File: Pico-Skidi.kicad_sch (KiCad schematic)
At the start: 10 parts, among them M1 Motor_DC, M2 Motor_DC, M3 Motor_DC, M4 Motor_Servo, M5 Motor_Servo, U1 Pico, U2 PDRV8411PWPR, U3 PDRV8411PWPR, U4 LM5156HPWPR

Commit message: Starting on Power
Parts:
- added C1: 10uf, symbol Device:C
- added D1: LED, symbol Device:LED
- added J1: BAT, symbol Connector_Generic:Conn_01x02
- added J2: RGBLED, symbol Connector_Generic:Conn_01x03
- added J3: USB_C_Receptacle, symbol Connector:USB_C_Receptacle
- added R1, R2: 5k1, symbol Device:R
- added R3: 2k, symbol Device:R
- added U5: MCP73831T-2ACI/OT, SOT-23-5_MC_MCH, symbol MCP73831:MCP73831T-2ACI_OT
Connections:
- net GND: now reaches U2.11 (GND)
- net GND: now also M4.3 (-), M5.3 (-), U1.13 (GND), U1.18 (GND), U1.23 (GND), U1.28 (GND), U1.3 (GND), U1.33 (AGND), U1.38 (GND), U1.42 (GND), U1.8 (GND), U3.11 (GND), C1.2, J2.3 (Pin_3), J3.A1 (GND), J3.A12 (GND), J3.B1 (GND), J3.B12 (GND), J3.S1 (SHIELD), R1.2, R2.2, U5.2 (VSS)
- new net: D1.1 (K), R3.1
- new net: J3.A5 (CC1), R2.1
- new net: J3.B5 (CC2), R1.1
- new net: R3.2, U5.1 (STAT)
- new net: J1.1 (Pin_1), U5.3 (VBAT)
- new net D+: J3.A6 (D+), J3.B6 (D+)
- new net D-: J3.A7 (D-), J3.B7 (D-)
- new net VBUS: C1.1, D1.2 (A), J3.A4 (VBUS), J3.A9 (VBUS), J3.B4 (VBUS), J3.B9 (VBUS), U5.4 (VDD)
- no-connect marks 0 -> 10
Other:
- moved on the sheet: M1, M2, M3, M4, M5, U1, U2, U3, U4

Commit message: Sync
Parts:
- added R4, R5: R, symbol Device:R
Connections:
- net PROG: now reaches U5.5 (PROG)
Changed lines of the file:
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@@
     (stroke (width 0) (type default))
+  )
+  (label "PROG" (at 87.63 21.59 180) (fields_autoplaced)
+    (effects (font (size 1.27 1.27)) (justify right bottom))
   )
   (label "D+" (at 41.91 43.18 0) (fields_autoplaced)
@@
     )
   )
+  (symbol (lib_id "Device:R") (at 71.12 66.04 0) (unit 1)
+    (in_bom yes) (on_board yes) (dnp no) (fields_autoplaced)
+    (property "Reference" "R5" (at 73.66 64.77 0)
+      (effects (font (size 1.27 1.27)) (justify left))
+    )
+    (property "Value" "R" (at 73.66 67.31 0)
+      (effects (font (size 1.27 1.27)) (justify left))
+    )
+    (property "Footprint" "" (at 69.342 66.04 90)
+      (effects (font (size 1.27 1.27)) hide)
+    )
+    (property "Datasheet" "~" (at 71.12 66.04 0)
+      (effects (font (size 1.27 1.27)) hide)
+    )
+    (pin "1")
+    (pin "2")
+    (instances
+      (project "Pico-Skidi"
+        (path "/21865b85-eb74-4d61-a31a-30858d3bc341"
+          (reference "R5") (unit 1)
+        )
+      )
+    )
+  )
   (symbol (lib_id "Device:C") (at 81.28 48.26 0) (unit 1)
     (in_bom yes) (on_board yes) (dnp no) (fields_autoplaced)
@@
         )
       )
+    )
+  )
+  (symbol (lib_id "Device:R") (at 60.96 66.04 0) (unit 1)
+    (in_bom yes) (on_board yes) (dnp no) (fields_autoplaced)
+    (property "Reference" "R4" (at 63.5 64.77 0)
+      (effects (font (size 1.27 1.27)) (justify left))
+    )
+    (property "Value" "R" (at 63.5 67.31 0)
+      (effects (font (size 1.27 1.27)) (justify left))
+    )
+    (property "Footprint" "" (at 59.182 66.04 90)
+      (effects (font (size 1.27 1.27)) hide)
+    )
+    (property "Datasheet" "~" (at 60.96 66.04 0)
+      (effects (font (size 1.27 1.27)) hide)
+    )
+    (pin "1")
+    (pin "2")
+    (instances
+      (project "Pico-Skidi"
+        (path "/21865b85-eb74-4d61-a31a-30858d3bc341"
+          (reference "R4") (unit 1)
+        )
+      )

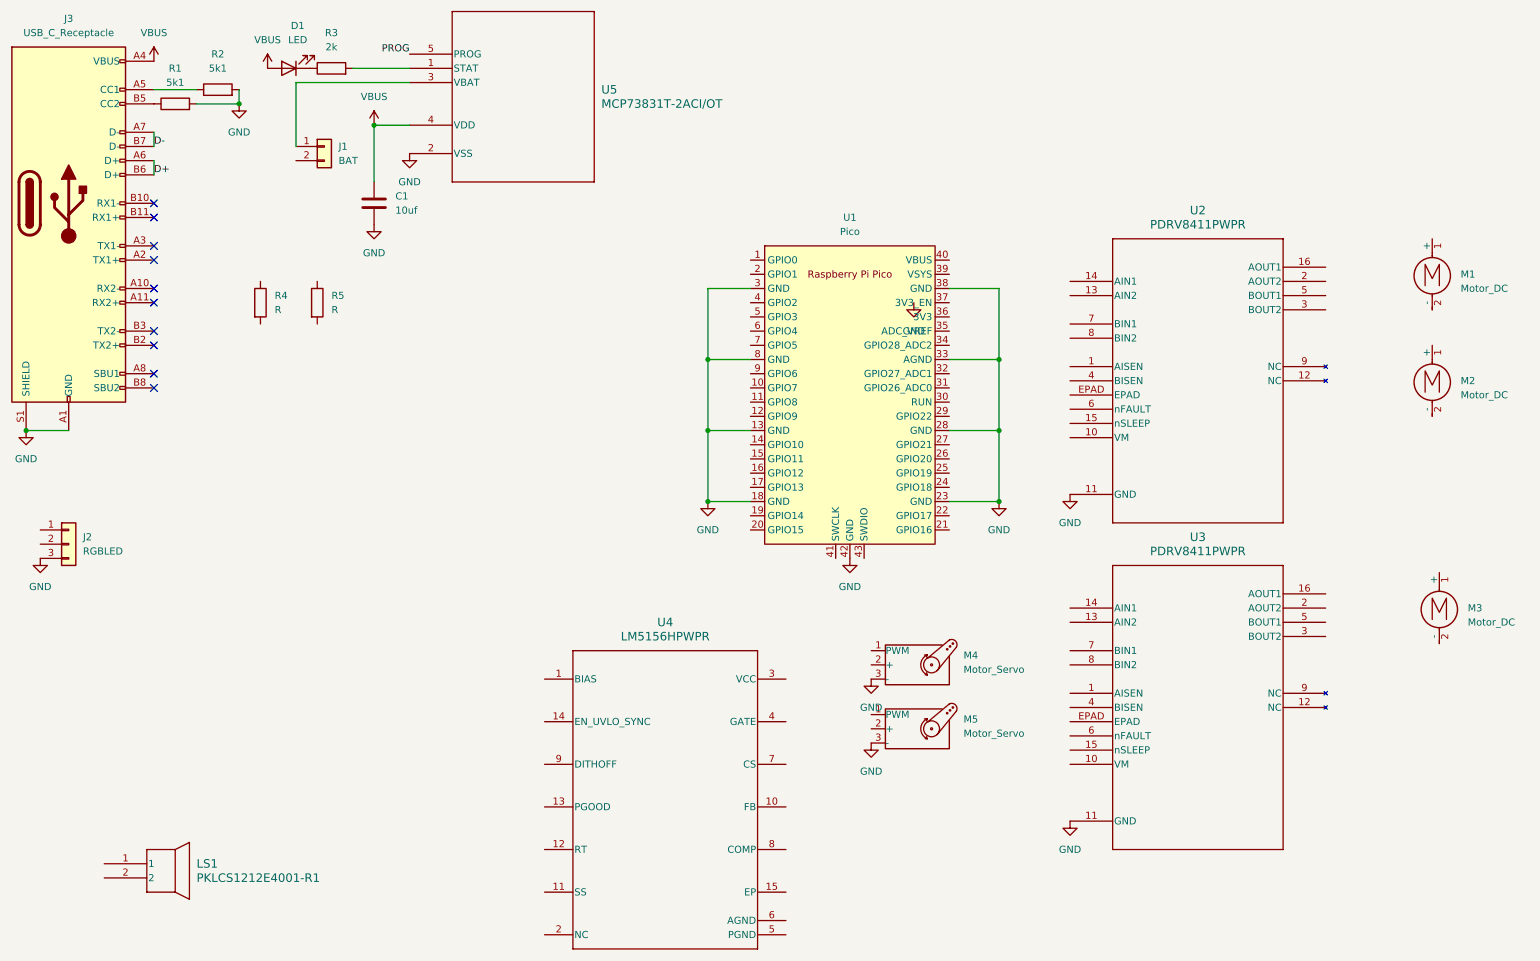
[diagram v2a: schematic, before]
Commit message: Additional sheets in the schematic
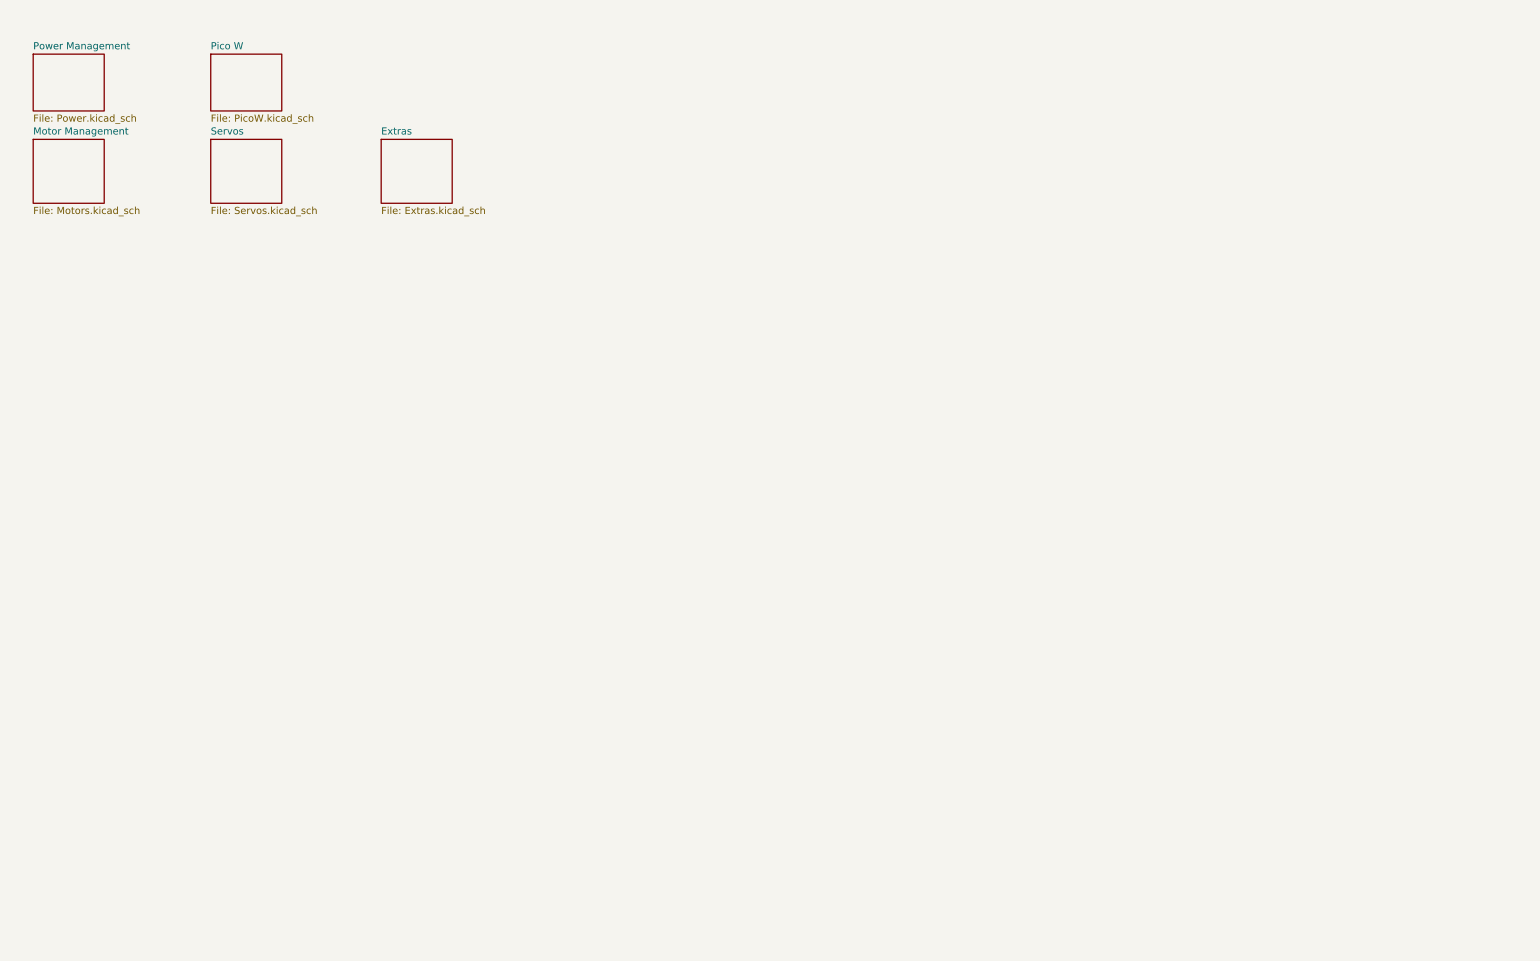
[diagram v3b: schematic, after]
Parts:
- removed C1: 10uf, symbol Device:C
- removed D1: LED, symbol Device:LED
- removed J1: BAT, symbol Connector_Generic:Conn_01x02
- removed J2: RGBLED, symbol Connector_Generic:Conn_01x03
- removed J3: USB_C_Receptacle, symbol Connector:USB_C_Receptacle
- removed LS1: PKLCS1212E4001-R1, PKLCS_472x472_MUR, symbol PKLCS1212E4001:PKLCS1212E4001-R1
- removed M1, M2, M3: Motor_DC, symbol Motor:Motor_DC
- removed M4, M5: Motor_Servo, symbol Motor:Motor_Servo
- removed R1, R2: 5k1, symbol Device:R
- removed R3: 2k, symbol Device:R
- removed R4, R5: R, symbol Device:R
- removed U1: Pico, RPi_Pico:RPi_Pico_SMD_TH, symbol MCU_RaspberryPi_and_Boards:Pico
- removed U2, U3: PDRV8411PWPR, TSSOP_11PWPR_TEX, symbol DRV8411:PDRV8411PWPR
- removed U4: LM5156HPWPR, PWP0014H-IPC_A, symbol LM5156H:LM5156HPWPR
- removed U5: MCP73831T-2ACI/OT, SOT-23-5_MC_MCH, symbol MCP73831:MCP73831T-2ACI_OT
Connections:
- no-connect marks 10 -> 0
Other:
- added sheet Extras (Extras.kicad_sch)
- added sheet Motor Management (Motors.kicad_sch)
- added sheet Pico W (PicoW.kicad_sch)
- added sheet Power Management (Power.kicad_sch)
- added sheet Servos (Servos.kicad_sch)

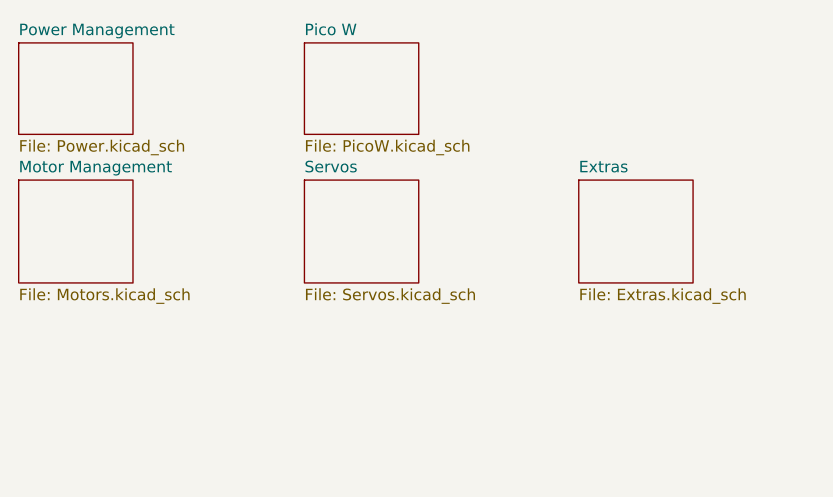
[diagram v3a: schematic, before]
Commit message: Adding pins for Pico
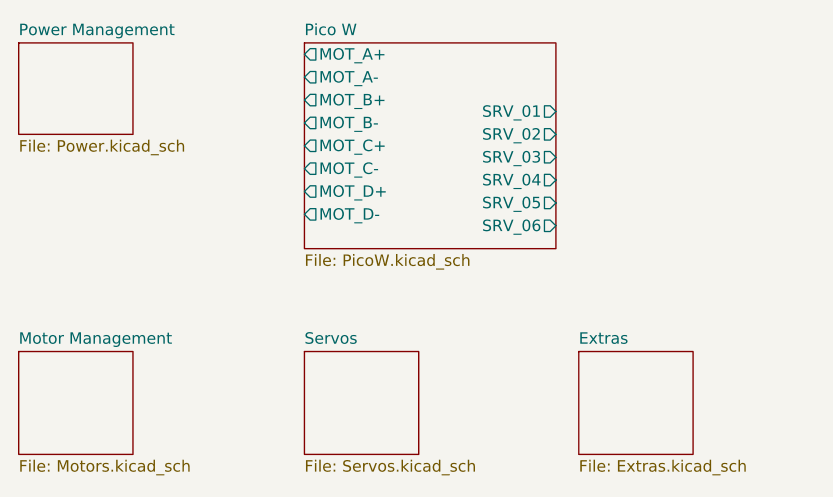
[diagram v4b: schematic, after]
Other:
- sheet Pico W ports: added MOT_A+, MOT_A-, MOT_B+, MOT_B-, MOT_C+, MOT_C-, MOT_D+, MOT_D-, SRV_01, SRV_02, SRV_03, SRV_04, SRV_05, SRV_06; removed none
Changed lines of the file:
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@@
 (kicad_sch (version 20230121) (generator eeschema)
   (paper "A4")
-  (sheet (at 52.07 21.59) (size 12.7 10.16) (fields_autoplaced)
+  (sheet (at 52.07 21.59) (size 27.94 22.86) (fields_autoplaced)
     (stroke (width 0.1524) (type solid))
     (fill (color 0 0 0 0.0000))
@@
       (effects (font (size 1.27 1.27)) (justify left bottom))
     )
-    (property "Sheetfile" "PicoW.kicad_sch" (at 52.07 32.3346 0)
+    (property "Sheetfile" "PicoW.kicad_sch" (at 52.07 45.0346 0)
       (effects (font (size 1.27 1.27)) (justify left top))
+    )
+    (pin "MOT_D+" output (at 52.07 38.1 180)
+      (effects (font (size 1.27 1.27)) (justify left))
+    )
+    (pin "MOT_D-" output (at 52.07 40.64 180)
+      (effects (font (size 1.27 1.27)) (justify left))
+    )
+    (pin "MOT_B+" output (at 52.07 27.94 180)
+      (effects (font (size 1.27 1.27)) (justify left))
+    )
+    (pin "MOT_B-" output (at 52.07 30.48 180)
+      (effects (font (size 1.27 1.27)) (justify left))
+    )
+    (pin "MOT_A+" output (at 52.07 22.86 180)
+      (effects (font (size 1.27 1.27)) (justify left))
+    )
+    (pin "SRV_05" output (at 80.01 39.37 0)
+      (effects (font (size 1.27 1.27)) (justify right))
+    )
+    (pin "SRV_06" output (at 80.01 41.91 0)
+      (effects (font (size 1.27 1.27)) (justify right))
+    )
+    (pin "SRV_01" output (at 80.01 29.21 0)
+      (effects (font (size 1.27 1.27)) (justify right))
+    )
+    (pin "SRV_02" output (at 80.01 31.75 0)
+      (effects (font (size 1.27 1.27)) (justify right))
+    )
+    (pin "SRV_03" output (at 80.01 34.29 0)
+      (effects (font (size 1.27 1.27)) (justify right))
+    )
+    (pin "SRV_04" output (at 80.01 36.83 0)
+      (effects (font (size 1.27 1.27)) (justify right))
+    )
+    (pin "MOT_C+" output (at 52.07 33.02 180)
+      (effects (font (size 1.27 1.27)) (justify left))
+    )
+    (pin "MOT_A-" output (at 52.07 25.4 180)
+      (effects (font (size 1.27 1.27)) (justify left))
+    )
+    (pin "MOT_C-" output (at 52.07 35.56 180)
+      (effects (font (size 1.27 1.27)) (justify left))
     )
     (instances
@@
     )
   )
-  (sheet (at 82.55 36.83) (size 12.7 11.43) (fields_autoplaced)
+  (sheet (at 82.55 55.88) (size 12.7 11.43) (fields_autoplaced)
     (stroke (width 0.1524) (type solid))
     (fill (color 0 0 0 0.0000))
-    (property "Sheetname" "Extras" (at 82.55 36.1184 0)
+    (property "Sheetname" "Extras" (at 82.55 55.1684 0)
       (effects (font (size 1.27 1.27)) (justify left bottom))
     )
-    (property "Sheetfile" "Extras.kicad_sch" (at 82.55 48.8446 0)
+    (property "Sheetfile" "Extras.kicad_sch" (at 82.55 67.8946 0)
       (effects (font (size 1.27 1.27)) (justify left top))
     )
@@
     )
   )
-  (sheet (at 20.32 36.83) (size 12.7 11.43) (fields_autoplaced)
+  (sheet (at 20.32 55.88) (size 12.7 11.43) (fields_autoplaced)
     (stroke (width 0.1524) (type solid))
     (fill (color 0 0 0 0.0000))
-    (property "Sheetname" "Motor Management" (at 20.32 36.1184 0)
+    (property "Sheetname" "Motor Management" (at 20.32 55.1684 0)
       (effects (font (size 1.27 1.27)) (justify left bottom))
     )
-    (property "Sheetfile" "Motors.kicad_sch" (at 20.32 48.8446 0)
+    (property "Sheetfile" "Motors.kicad_sch" (at 20.32 67.8946 0)
       (effects (font (size 1.27 1.27)) (justify left top))
     )
@@
     )
   )
-  (sheet (at 52.07 36.83) (size 12.7 11.43) (fields_autoplaced)
+  (sheet (at 52.07 55.88) (size 12.7 11.43) (fields_autoplaced)
     (stroke (width 0.1524) (type solid))
     (fill (color 0 0 0 0.0000))
-    (property "Sheetname" "Servos" (at 52.07 36.1184 0)
+    (property "Sheetname" "Servos" (at 52.07 55.1684 0)
       (effects (font (size 1.27 1.27)) (justify left bottom))
     )
-    (property "Sheetfile" "Servos.kicad_sch" (at 52.07 48.8446 0)
+    (property "Sheetfile" "Servos.kicad_sch" (at 52.07 67.8946 0)
       (effects (font (size 1.27 1.27)) (justify left top))
     )

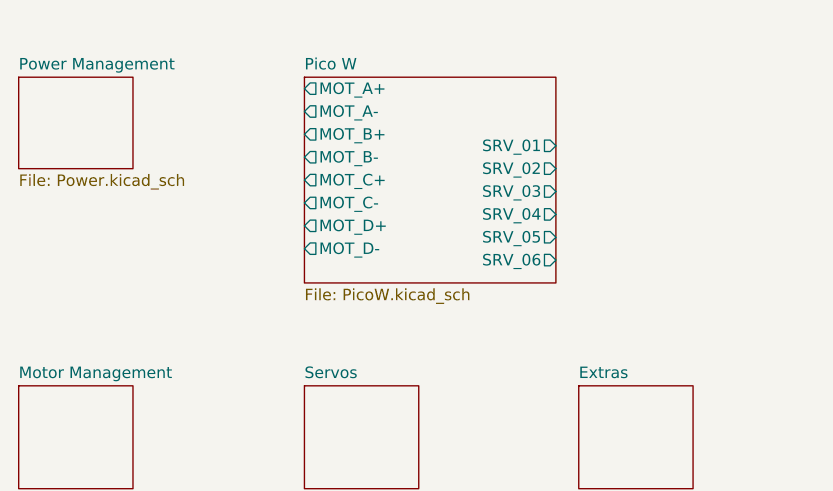
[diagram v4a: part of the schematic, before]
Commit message: Additional sheets in the schematic
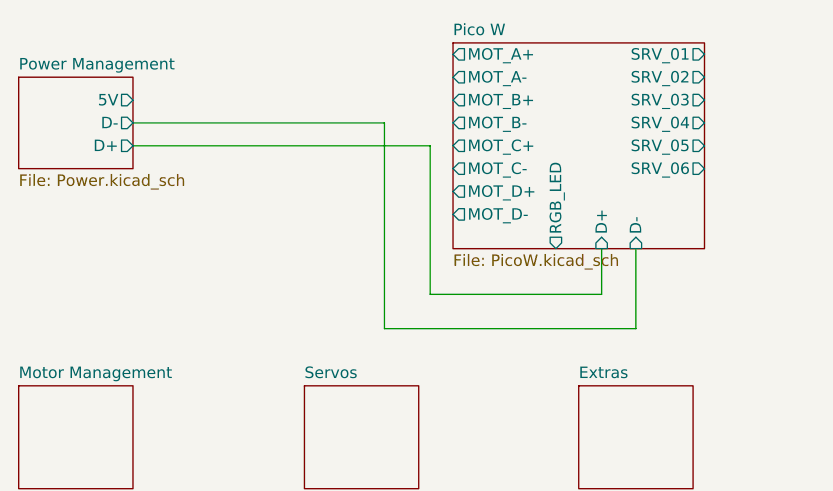
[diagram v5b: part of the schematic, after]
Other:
- sheet Pico W ports: added D+, D-, RGB_LED; removed none
- sheet Power Management ports: added 5V, D+, D-; removed none
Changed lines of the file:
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@@
 (kicad_sch (version 20230121) (generator eeschema)
   (paper "A4")
-  (sheet (at 52.07 21.59) (size 27.94 22.86) (fields_autoplaced)
+  (wire (pts (xy 33.02 29.21) (xy 66.04 29.21))
+    (stroke (width 0) (type default))
+  )
+  (wire (pts (xy 85.09 45.72) (xy 85.09 40.64))
+    (stroke (width 0) (type default))
+  )
+  (wire (pts (xy 66.04 45.72) (xy 85.09 45.72))
+    (stroke (width 0) (type default))
+  )
+  (wire (pts (xy 60.96 26.67) (xy 33.02 26.67))
+    (stroke (width 0) (type default))
+  )
+  (wire (pts (xy 60.96 49.53) (xy 60.96 26.67))
+    (stroke (width 0) (type default))
+  )
+  (wire (pts (xy 66.04 29.21) (xy 66.04 45.72))
+    (stroke (width 0) (type default))
+  )
+  (wire (pts (xy 60.96 49.53) (xy 88.9 49.53))
+    (stroke (width 0) (type default))
+  )
+  (wire (pts (xy 88.9 49.53) (xy 88.9 40.64))
+    (stroke (width 0) (type default))
+  )
+  (sheet (at 68.58 17.78) (size 27.94 22.86) (fields_autoplaced)
     (stroke (width 0.1524) (type solid))
     (fill (color 0 0 0 0.0000))
-    (property "Sheetname" "Pico W" (at 52.07 20.8784 0)
+    (property "Sheetname" "Pico W" (at 68.58 17.0684 0)
       (effects (font (size 1.27 1.27)) (justify left bottom))
     )
-    (property "Sheetfile" "PicoW.kicad_sch" (at 52.07 45.0346 0)
+    (property "Sheetfile" "PicoW.kicad_sch" (at 68.58 41.2246 0)
       (effects (font (size 1.27 1.27)) (justify left top))
     )
-    (pin "MOT_D+" output (at 52.07 38.1 180)
+    (pin "MOT_D+" output (at 68.58 34.29 180)
       (effects (font (size 1.27 1.27)) (justify left))
     )
-    (pin "MOT_D-" output (at 52.07 40.64 180)
+    (pin "MOT_D-" output (at 68.58 36.83 180)
       (effects (font (size 1.27 1.27)) (justify left))
     )
-    (pin "MOT_B+" output (at 52.07 27.94 180)
+    (pin "MOT_B+" output (at 68.58 24.13 180)
       (effects (font (size 1.27 1.27)) (justify left))
     )
-    (pin "MOT_B-" output (at 52.07 30.48 180)
+    (pin "MOT_B-" output (at 68.58 26.67 180)
       (effects (font (size 1.27 1.27)) (justify left))
     )
-    (pin "MOT_A+" output (at 52.07 22.86 180)
+    (pin "MOT_A+" output (at 68.58 19.05 180)
       (effects (font (size 1.27 1.27)) (justify left))
     )
-    (pin "SRV_05" output (at 80.01 39.37 0)
+    (pin "SRV_05" output (at 96.52 29.21 0)
       (effects (font (size 1.27 1.27)) (justify right))
     )
-    (pin "SRV_06" output (at 80.01 41.91 0)
+    (pin "SRV_06" output (at 96.52 31.75 0)
       (effects (font (size 1.27 1.27)) (justify right))
     )
-    (pin "SRV_01" output (at 80.01 29.21 0)
+    (pin "SRV_01" output (at 96.52 19.05 0)
       (effects (font (size 1.27 1.27)) (justify right))
     )
-    (pin "SRV_02" output (at 80.01 31.75 0)
+    (pin "SRV_02" output (at 96.52 21.59 0)
       (effects (font (size 1.27 1.27)) (justify right))
     )
-    (pin "SRV_03" output (at 80.01 34.29 0)
+    (pin "SRV_03" output (at 96.52 24.13 0)
       (effects (font (size 1.27 1.27)) (justify right))
     )
-    (pin "SRV_04" output (at 80.01 36.83 0)
+    (pin "SRV_04" output (at 96.52 26.67 0)
       (effects (font (size 1.27 1.27)) (justify right))
     )
-    (pin "MOT_C+" output (at 52.07 33.02 180)
+    (pin "MOT_C+" output (at 68.58 29.21 180)
       (effects (font (size 1.27 1.27)) (justify left))
     )
-    (pin "MOT_A-" output (at 52.07 25.4 180)
+    (pin "MOT_A-" output (at 68.58 21.59 180)
       (effects (font (size 1.27 1.27)) (justify left))
     )
-    (pin "MOT_C-" output (at 52.07 35.56 180)
+    (pin "MOT_C-" output (at 68.58 31.75 180)
+      (effects (font (size 1.27 1.27)) (justify left))
+    )
+    (pin "RGB_LED" output (at 80.01 40.64 270)
+      (effects (font (size 1.27 1.27)) (justify left))
+    )
+    (pin "D+" input (at 85.09 40.64 270)
+      (effects (font (size 1.27 1.27)) (justify left))
+    )
+    (pin "D-" input (at 88.9 40.64 270)
       (effects (font (size 1.27 1.27)) (justify left))
     )
@@
       (effects (font (size 1.27 1.27)) (justify left top))
     )
+    (pin "D-" output (at 33.02 26.67 0)
+      (effects (font (size 1.27 1.27)) (justify right))
+    )
+    (pin "D+" output (at 33.02 29.21 0)
+      (effects (font (size 1.27 1.27)) (justify right))
+    )
+    (pin "5V" output (at 33.02 24.13 0)
+      (effects (font (size 1.27 1.27)) (justify right))
+    )
     (instances

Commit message: Lots of changes
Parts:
- added SW1: BOOTSEL, symbol Switch:SW_SPST
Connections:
- new net GND: SW1.2 (B)
- new net Pico W/BOOTSEL: SW1.1 (A)
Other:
- sheet Extras ports: added BUZZER, RGB_LED; removed none
- sheet Motor Management ports: added MOT_A+, MOT_A-, MOT_B+, MOT_B-, MOT_C+, MOT_C-, MOT_D+, MOT_D-, nFAULT_01, nFAULT_02; removed none
- sheet Pico W ports: added BOOTSEL, BUZZER, USB_D+, USB_D-, nFAULT_01, nFAULT_02; removed D+, D-
- sheet Power Management ports: added none; removed 5V
- sheet Servos ports: added SRV_01, SRV_02, SRV_03, SRV_04, SRV_05, SRV_06; removed none
